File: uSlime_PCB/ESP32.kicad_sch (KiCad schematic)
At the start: 14 parts, among them U4 ESP32-C6-MINI-1

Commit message: Change charge LED to 2.2k, always on light if not charging
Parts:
- R9: value 1k -> 2.2k
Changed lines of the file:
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@@
 			)
 		)
-		(property "Value" "1k"
+		(property "Value" "2.2k"
 			(at 200.6599 59.69 0)
 			(effects

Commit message: v1.1.0 - Add 603 LED and resistor for charger status
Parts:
- R9: value 2.2k -> 1k
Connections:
- net STAT is gone; now on net IO19/SCK: R9.1
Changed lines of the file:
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@@
 	(wire
 		(pts
-			(xy 204.47 62.23) (xy 203.2 62.23)
+			(xy 210.82 62.23) (xy 203.2 62.23)
 		)
 		(stroke
@@
 		)
 	)
+	(label "IO19/SCK"
+		(at 210.82 62.23 180)
+		(fields_autoplaced yes)
+		(effects
+			(font
+				(size 0.889 0.889)
+			)
+			(justify right bottom)
+		)
+	)
 	(label "IO17/RX"
 		(at 137.16 115.57 0)
@@
 		(property "Intersheetrefs" "${INTERSHEET_REFS}"
 			(at 157.7437 80.01 0)
-			(effects
-				(font
-					(size 1.27 1.27)
-				)
-				(justify left)
-				(hide yes)
-			)
-		)
-	)
-	(global_label "STAT"
-		(shape input)
-		(at 204.47 62.23 0)
-		(fields_autoplaced yes)
-		(effects
-			(font
-				(size 1.27 1.27)
-			)
-			(justify left)
-		)
-		(property "Intersheetrefs" "${INTERSHEET_REFS}"
-			(at 211.6885 62.23 0)
 			(effects
 				(font
@@
 			)
 		)
-		(property "Value" "2.2k"
+		(property "Value" "1k"
 			(at 200.6599 59.69 0)
 			(effects

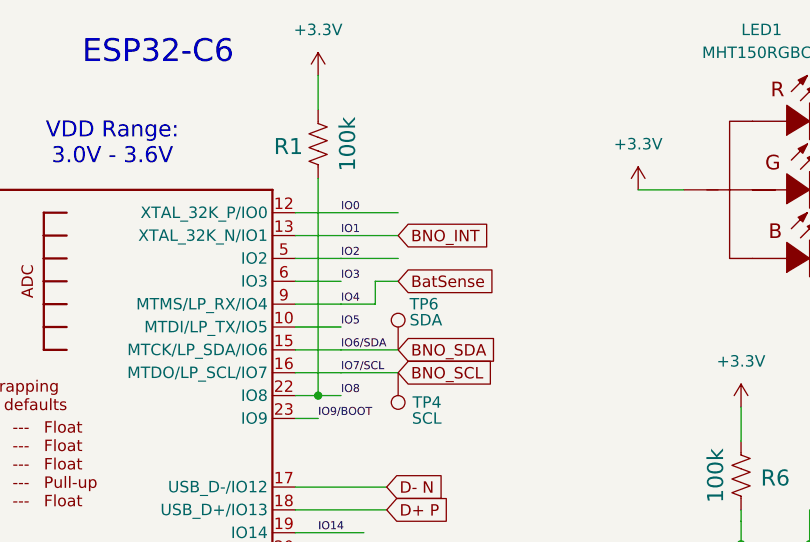
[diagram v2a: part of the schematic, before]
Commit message: v1.2.0 - Refactor component placement and electrical accuracy
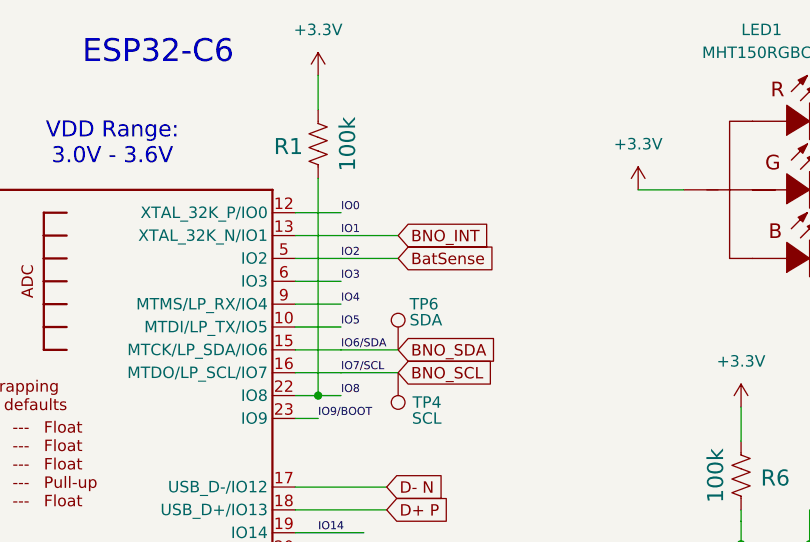
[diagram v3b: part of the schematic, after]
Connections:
- net IO2 is gone; now on net BatSense: U4.5 (IO2)
- net BatSense: no longer U4.9 (MTMS/LP_RX/IO4)
- new net IO4: U4.9 (MTMS/LP_RX/IO4)
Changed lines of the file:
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@@
-	(wire
-		(pts
-			(xy 143.51 82.55) (xy 139.7 82.55)
-		)
-		(stroke
-			(width 0)
-			(type default)
-		)
-	)
 	(wire
 		(pts
@@
 	(wire
 		(pts
-			(xy 146.05 80.01) (xy 143.51 80.01)
-		)
-		(stroke
-			(width 0)
-			(type default)
-		)
-	)
-	(wire
-		(pts
 			(xy 134.62 77.47) (xy 139.7 77.47)
 		)
@@
 	(wire
 		(pts
-			(xy 143.51 80.01) (xy 143.51 82.55)
-		)
-		(stroke
-			(width 0)
-			(type default)
-		)
-	)
-	(wire
-		(pts
 			(xy 137.16 110.49) (xy 144.78 110.49)
 		)
@@
 	(wire
 		(pts
-			(xy 134.62 72.39) (xy 146.05 72.39)
-		)
-		(stroke
-			(width 0.1524)
-			(type solid)
+			(xy 134.62 72.39) (xy 139.7 72.39)
+		)
+		(stroke
+			(width 0)
+			(type default)
 		)
 	)
@@
 		)
 	)
-	(global_label "BatSense"
-		(shape input)
-		(at 146.05 80.01 0)
-		(fields_autoplaced yes)
-		(effects
-			(font
-				(size 1.27 1.27)
-			)
-			(justify left)
-		)
-		(property "Intersheetrefs" "${INTERSHEET_REFS}"
-			(at 157.7437 80.01 0)
-			(effects
-				(font
-					(size 1.27 1.27)
-				)
-				(justify left)
-				(hide yes)
-			)
-		)
-	)
 	(global_label "BNO_INT2"
 		(shape input)
@@
 			(effects
 				(font
+					(size 1.27 1.27)
+				)
+				(justify left)
+				(hide yes)
+			)
+		)
+	)
+	(global_label "BatSense"
+		(shape input)
+		(at 146.05 77.47 0)
+		(fields_autoplaced yes)
+		(effects
+			(font
+				(size 1.27 1.27)
+			)
+			(justify left)
+		)
+		(property "Intersheetrefs" "${INTERSHEET_REFS}"
+			(at 157.7437 77.47 0)
+			(effects
+				(font
